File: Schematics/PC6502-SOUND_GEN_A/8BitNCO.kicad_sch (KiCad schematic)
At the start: 11 parts, among them IC1 AS7C164A-15PCN, IC2 AS7C164A-15PCN, U1 74LS283, U15 74HCT574, U3 74LS283, U8 74HC74

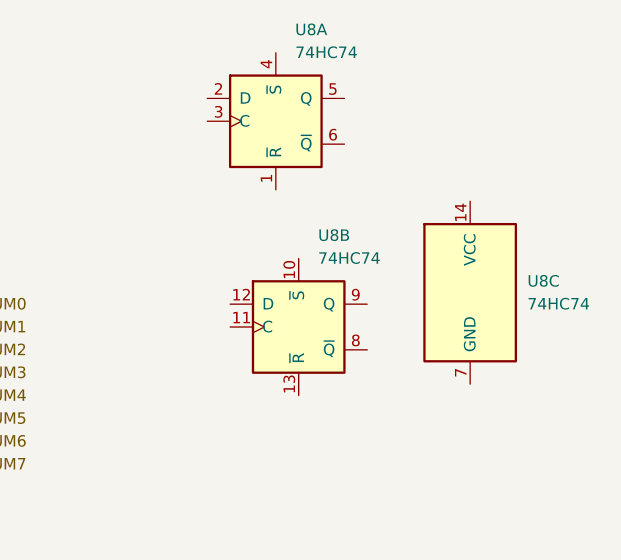
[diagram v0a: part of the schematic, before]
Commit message: Created V1.1 Schematic and PCB
A LOT of changes from v1.00;
removed clock stretcher (will now live in the CPLD)
moved the USB interface direct to the PCB
changed power pins
Added extra capacitance
Used Grant Searle's OSI basic and memory map to bring up the board
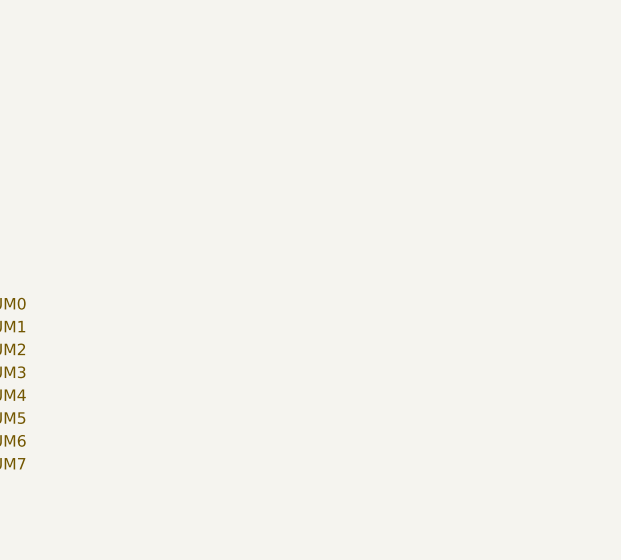
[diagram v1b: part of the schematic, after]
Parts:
- removed U8: 74HC74, symbol 74xx:74HC74

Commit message: Update KeyTFT CPLD
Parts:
- added J4: Conn_01x09, Connector_PinSocket_2.54mm:PinSocket_1x09_P2.54mm_Vertical, symbol Connector_Generic:Conn_01x09
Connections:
- net ACC_DQ0: now also J4.2 (Pin_2)
- net ACC_DQ1: now also J4.3 (Pin_3)
- net ACC_DQ2: now also J4.4 (Pin_4)
- net ACC_DQ3: now also J4.5 (Pin_5)
- net ACC_DQ4: now also J4.6 (Pin_6)
- net ACC_DQ5: now also J4.7 (Pin_7)
- net ACC_DQ6: now also J4.8 (Pin_8)
- net ACC_DQ7: now also J4.9 (Pin_9)
- net GND: now also J4.1 (Pin_1)
